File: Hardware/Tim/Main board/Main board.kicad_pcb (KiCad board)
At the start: 4 copper layers, 120.9 x 66.6 mm, 184 parts, among them J1 SOICbite, J10 Conn_01x03_Socket, J11 Conn_01x02_Pin, J12 USB_C_Receptacle_USB2.0, J13 Conn_01x02_Socket, J14 Conn_01x02_Pin, J15 Conn_01x04_Socket, J16 Conn_01x02_Pin, J17 Conn_01x04_Pin, J18 Conn_01x03_Socket, J2 USB_C_Receptacle_USB2.0, J3 Conn_01x04_Socket, J4 Conn_01x04_Socket, J5 Conn_01x04_Socket, J6 Conn_01x02_Socket, J7 Conn_01x02_Socket, J8 U.FL, J9 SOICbite, Q1 IRLML0060TRPBF, Q2 IRLML0060TRPBF, U1 RP2040, U10 MAX-M10S, U11 ADP7105ACPZ-5.0-R7, U12 ADP7105ACPZ-3.3-R7, U13 ADP7105ACPZ-5.0-R7, U14 TPS2121RUXR, U15 TPS2121RUXR, U2 W25Q64JVZP, U3 MS5607-02BA, U4 BMI270, U5 ADP7105ACPZ-3.3-R7, U6 DRF1262TL, U7 RP2040, U8 W25Q64JVZP, Y1 12MHz, Y2 12MHz

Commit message: Double checking everything is pushed
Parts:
- added J19: Micro_SD_Card, BPPlib:JAE_ST1W008S4ER1500, F.Cu at (99.0, 108.8)
- added J20: Micro_SD_Card, BPPlib:JAE_ST1W008S4ER1500, F.Cu at (154.6, 102.0)
- added REF**: MountingHole_3.2mm_M3, MountingHole:MountingHole_3.2mm_M3, F.Cu at (174.0, 83.0)
- moved AE1 38.2 mm to (59.2, 114.5), turned to -90 degrees
- moved J15 34.3 mm to (96.4, 114.8), turned to 0 degrees
- moved JP3 29.5 mm to (98.2, 110.2)
- moved J18 29.1 mm to (84.2, 114.5), turned to 0 degrees
- moved JP4 26.5 mm to (94.3, 110.2), turned to 180 degrees
- moved REF** 26.4 mm to (131.0, 105.0)
- moved U10 25.3 mm to (73.2, 113.8), turned to 180 degrees
- moved J7 24.3 mm to (61.8, 102.2), turned to -90 degrees
- moved J6 24.0 mm to (61.8, 93.5), turned to -90 degrees
- moved C57 20.0 mm to (70.8, 107.4), turned to 180 degrees
- moved R63 19.3 mm to (65.6, 92.8), turned to -90 degrees
- moved R44 18.6 mm to (65.7, 101.4), turned to -90 degrees
- moved BT1 15.2 mm to (72.1, 103.5), turned to -90 degrees
- moved C59 14.2 mm to (82.0, 101.0), turned to 180 degrees
- moved R12 13.8 mm to (76.8, 106.5), turned to 180 degrees
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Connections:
- U1 pad 32: /TXEN -> /SPI0_CS_SD
- U1 pad 38: /EXTINT -> /TXEN
- U7 pad 15: unconnected-(U7-GPIO12-Pad15) -> /SPI0_POCI_R
- U7 pad 16: unconnected-(U7-GPIO13-Pad16) -> /SPI0_CS_SD_R
- U7 pad 17: unconnected-(U7-GPIO14-Pad17) -> /SPI0_SCK_R
- U7 pad 18: unconnected-(U7-GPIO15-Pad18) -> /SPI0_PICO_R
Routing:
- net /DIR: track 110.2 -> 59.2 mm, vias 6 -> 3
- net /STEP: track 107.7 -> 58.7 mm, vias 6 -> 3
- net GND: track 335.8 -> 384.0 mm, vias 41 -> 46
- net /SPI0_POCI_R: track 0.00 -> 42.9 mm
- net /EXTINT: track 42.0 -> 0.00 mm, vias 2 -> 0
- net /SPI0_CS_SD_R: track 0.00 -> 40.7 mm, vias 0 -> 2
- net /SPI0_CS_SD: track 0.00 -> 39.9 mm, vias 0 -> 2
- net /SPI0_SCK_R: track 0.00 -> 39.5 mm
- net /SPI0_PICO_R: track 0.00 -> 36.0 mm
- net /SPI0_PICO: track 39.1 -> 71.4 mm, vias 2 -> 3
- net /SPI0_SCK: track 41.8 -> 72.6 mm, vias 2 -> 4
- net /TIMEPULSE: track 42.9 -> 71.6 mm
- net +5V: track 81.5 -> 108.5 mm, vias 0 -> 4
- net /SPI0_POCI: track 35.5 -> 62.0 mm, vias 2 -> 3
- net Net-(J13-Pin_2): track 29.9 -> 55.3 mm, vias 2 -> 0
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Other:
- board size 120.9 x 66.6 mm -> 121 x 66.5 mm
- board text added: "WayWayWay"

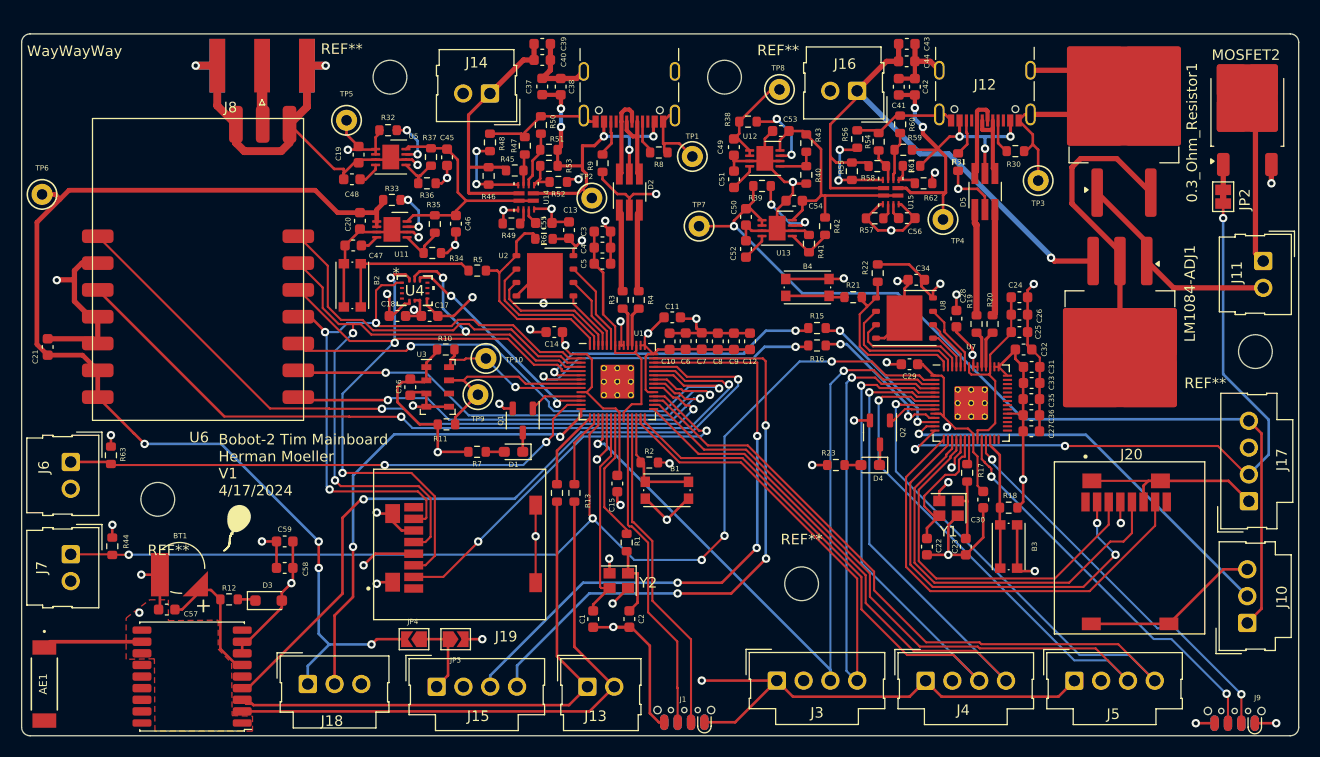
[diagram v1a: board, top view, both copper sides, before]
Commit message: Pressure temp done if so inclined add 2nd order compensation
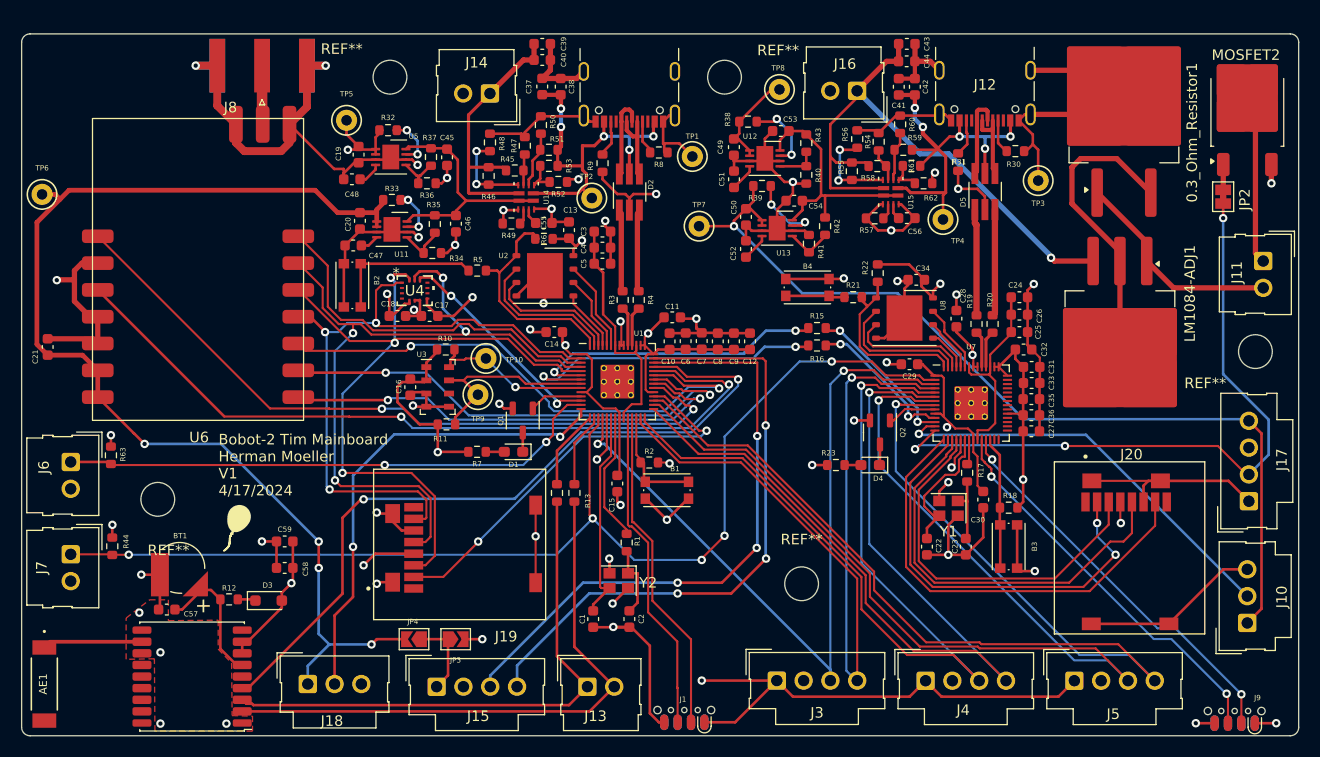
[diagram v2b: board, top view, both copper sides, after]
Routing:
- net GND: vias 46 -> 49
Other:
- board text removed: "WayWayWay"
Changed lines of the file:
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@@
 			(outputformat 1)
 			(mirror no)
-			(drillshape 1)
+			(drillshape 0)
 			(scaleselection 1)
-			(outputdirectory "")
+			(outputdirectory "./")
 		)
 	)
@@
 			(size 1.084435 1.084435)
 			(layers "F.Paste")
-			(roundrect_rratio 0.230535)
+			(roundrect_rratio 0.2305347946)
 		)
 		(pad "" smd roundrect
@@
 			(size 1.084435 1.084435)
 			(layers "F.Paste")
-			(roundrect_rratio 0.230535)
+			(roundrect_rratio 0.2305347946)
 		)
 		(pad "" smd roundrect
@@
 			(size 1.084435 1.084435)
 			(layers "F.Paste")
-			(roundrect_rratio 0.230535)
+			(roundrect_rratio 0.2305347946)
 		)
 		(pad "" smd roundrect
@@
 			(size 1.084435 1.084435)
 			(layers "F.Paste")
-			(roundrect_rratio 0.230535)
+			(roundrect_rratio 0.2305347946)
 		)
 		(pad "1" smd roundrect
@@
 			(layers "*.Cu" "*.Mask")
 			(remove_unused_layers no)
-			(roundrect_rratio 0.143678)
+			(roundrect_rratio 0.1436781609)
 			(net 9 "+5V")
 			(pinfunction "Pin_1")
@@
 			(layers "*.Cu" "*.Mask")
 			(remove_unused_layers no)
-			(roundrect_rratio 0.143678)
+			(roundrect_rratio 0.1436781609)
 			(net 16 "+BATT")
 			(pinfunction "Pin_1")
@@
 			(layers "*.Cu" "*.Mask")
 			(remove_unused_layers no)
-			(roundrect_rratio 0.143678)
+			(roundrect_rratio 0.1436781609)
 			(net 6 "+3V3")
 			(pinfunction "Pin_1")
@@
 			(size 1.084435 1.084435)
 			(layers "F.Paste")
-			(roundrect_rratio 0.230535)
+			(roundrect_rratio 0.2305347946)
 		)
 		(pad "" smd roundrect
@@
 			(size 1.084435 1.084435)
 			(layers "F.Paste")
-			(roundrect_rratio 0.230535)
+			(roundrect_rratio 0.2305347946)
 		)
 		(pad "" smd roundrect
@@
 			(size 1.084435 1.084435)
 			(layers "F.Paste")
-			(roundrect_rratio 0.230535)
+			(roundrect_rratio 0.2305347946)
 		)
 		(pad "" smd roundrect
@@
 			(size 1.084435 1.084435)
 			(layers "F.Paste")
-			(roundrect_rratio 0.230535)
+			(roundrect_rratio 0.2305347946)
 		)
 		(pad "1" smd roundrect
@@
 			(size 4.6 1.1)
 			(layers "F.Cu" "F.Paste" "F.Mask")
-			(roundrect_rratio 0.227273)
+			(roundrect_rratio 0.2272727273)
 			(net 170 "Net-(J11-Pin_2)")
 			(pinfunction "ADJ")
@@
 			(size 4.6 1.1)
 			(layers "F.Cu" "F.Paste" "F.Mask")
-			(roundrect_rratio 0.227273)
+			(roundrect_rratio 0.2272727273)
 			(net 169 "Net-(LM1084-ADJ1-VO)")
 			(pinfunction "VO")
@@
 			(size 4.55 5.25)
 			(layers "F.Cu" "F.Paste")
-			(roundrect_rratio 0.054945)
+			(roundrect_rratio 0.05494505495)
 			(net 169 "Net-(LM1084-ADJ1-VO)")
 			(pinfunction "VO")
@@
 			(size 4.55 5.25)
 			(layers "F.Cu" "F.Paste")
-			(roundrect_rratio 0.054945)
+			(roundrect_rratio 0.05494505495)
 			(net 169 "Net-(LM1084-ADJ1-VO)")
 			(pinfunction "VO")
@@
 			(size 9.4 10.8)
 			(layers "F.Cu" "F.Mask")
-			(roundrect_rratio 0.026596)
+			(roundrect_rratio 0.02659595745)
 			(net 169 "Net-(LM1084-ADJ1-VO)")
 			(pinfunction "VO")
@@
 			(size 4.55 5.25)
 			(layers "F.Cu" "F.Paste")
-			(roundrect_rratio 0.054945)
+			(roundrect_rratio 0.05494505495)
 			(net 169 "Net-(LM1084-ADJ1-VO)")
 			(pinfunction "VO")
@@
 			(size 4.55 5.25)
 			(layers "F.Cu" "F.Paste")
-			(roundrect_rratio 0.054945)
+			(roundrect_rratio 0.05494505495)
 			(net 169 "Net-(LM1084-ADJ1-VO)")
 			(pinfunction "VO")
@@
 			(size 4.6 1.1)
 			(layers "F.Cu" "F.Paste" "F.Mask")
-			(roundrect_rratio 0.227273)
+			(roundrect_rratio 0.2272727273)
 			(net 16 "+BATT")
 			(pinfunction "VI")
@@
 			(layers "*.Cu" "*.Mask")
 			(remove_unused_layers no)
-			(roundrect_rratio 0.143678)
+			(roundrect_rratio 0.1436781609)
 			(net 92 "/LS2")
 			(pinfunction "Pin_1")
@@
 			(size 2.2 1.2)
 			(layers "F.Cu" "F.Paste" "F.Mask")
-			(roundrect_rratio 0.208333)
+			(roundrect_rratio 0.2083333333)
 			(net 172 "Net-(JP2-B)")
 			(pinfunction "G")
@@
 			(size 3.05 2.75)
 			(layers "F.Cu" "F.Paste")
-			(roundrect_rratio 0.090909)
+			(roundrect_rratio 0.09090909091)
 			(net 171 "Net-(J11-Pin_1)")
 			(pinfunction "D")
@@
 			(size 3.05 2.75)
 			(layers "F.Cu" "F.Paste")
-			(roundrect_rratio 0.090909)
+			(roundrect_rratio 0.09090909091)
 			(net 171 "Net-(J11-Pin_1)")
 			(pinfunction "D")
@@
 			(size 6.4 5.8)
 			(layers "F.Cu" "F.Mask")
-			(roundrect_rratio 0.043103)
+			(roundrect_rratio 0.04310293103)
 			(net 171 "Net-(J11-Pin_1)")
 			(pinfunction "D")
@@
 			(size 3.05 2.75)
 			(layers "F.Cu" "F.Paste")
-			(roundrect_rratio 0.090909)
+			(roundrect_rratio 0.09090909091)
 			(net 171 "Net-(J11-Pin_1)")
 			(pinfunction "D")
@@
 			(size 3.05 2.75)
 			(layers "F.Cu" "F.Paste")
-			(roundrect_rratio 0.090909)
+			(roundrect_rratio 0.09090909091)
 			(net 171 "Net-(J11-Pin_1)")
 			(pinfunction "D")
@@
 			(size 2.2 1.2)
 			(layers "F.Cu" "F.Paste" "F.Mask")
-			(roundrect_rratio 0.208333)
+			(roundrect_rratio 0.2083333333)
 			(net 1 "GND")
 			(pinfunction "S")
@@
 			(layers "*.Cu" "*.Mask")
 			(remove_unused_layers no)
-			(roundrect_rratio 0.143678)
+			(roundrect_rratio 0.1436781609)
 			(net 148 "Net-(J14-Pin_1)")
 			(pinfunction "Pin_1")
@@
 			(size 1.37 1.73)
 			(layers "F.Paste")
-			(roundrect_rratio 0.182482)
+			(roundrect_rratio 0.1824817518)
 		)
 		(pad "" smd roundrect
@@
 			(size 1.37 1.73)
 			(layers "F.Paste")
-			(roundrect_rratio 0.182482)
+			(roundrect_rratio 0.1824817518)
 		)
 		(pad "" smd roundrect
@@
 			(size 1.37 1.73)
 			(layers "F.Paste")
-			(roundrect_rratio 0.182482)
+			(roundrect_rratio 0.1824817518)
 		)
 		(pad "" smd roundrect
@@
 			(size 1.37 1.73)
 			(layers "F.Paste")
-			(roundrect_rratio 0.182482)
+			(roundrect_rratio 0.1824817518)
 		)
 		(pad "1" smd roundrect
@@
 			(layers "*.Cu" "*.Mask")
 			(remove_unused_layers no)
-			(roundrect_rratio 0.143678)
+			(roundrect_rratio 0.1436781609)
 			(net 168 "+5V_R")
 			(pinfunction "Pin_1")
@@
 			(layers "*.Cu" "*.Mask")
 			(remove_unused_layers no)
-			(roundrect_rratio 0.143678)
+			(roundrect_rratio 0.1436781609)
 			(net 171 "Net-(J11-Pin_1)")
 			(pinfunction "Pin_1")
@@
 			(size 4.6 1.1)
 			(layers "F.Cu" "F.Paste" "F.Mask")
-			(roundrect_rratio 0.227273)
+			(roundrect_rratio 0.2272727273)
 			(net 170 "Net-(J11-Pin_2)")
 			(pintype "passive")
@@
 			(size 4.6 1.1)
 			(layers "F.Cu" "F.Paste" "F.Mask")
-			(roundrect_rratio 0.227273)
+			(roundrect_rratio 0.2272727273)
 			(net 169 "Net-(LM1084-ADJ1-VO)")
 			(pintype "passive")
@@
 			(size 4.55 5.25)
 			(layers "F.Cu" "F.Paste")
-			(roundrect_rratio 0.054945)
+			(roundrect_rratio 0.05494505495)
 			(net 1 "GND")
 			(pinfunction "Gnd")
@@
 			(size 4.55 5.25)
 			(layers "F.Cu" "F.Paste")
-			(roundrect_rratio 0.054945)
+			(roundrect_rratio 0.05494505495)
 			(net 1 "GND")
 			(pinfunction "Gnd")
@@
 			(size 9.4 10.8)
 			(layers "F.Cu" "F.Mask")
-			(roundrect_rratio 0.026596)
+			(roundrect_rratio 0.02659595745)
 			(net 1 "GND")
 			(pinfunction "Gnd")
@@
 			(size 4.55 5.25)
 			(layers "F.Cu" "F.Paste")
-			(roundrect_rratio 0.054945)
+			(roundrect_rratio 0.05494505495)
 			(net 1 "GND")
 			(pinfunction "Gnd")
@@
 			(size 4.55 5.25)
 			(layers "F.Cu" "F.Paste")
-			(roundrect_rratio 0.054945)
+			(roundrect_rratio 0.05494505495)
 			(net 1 "GND")
 			(pinfunction "Gnd")
@@
 			(layers "*.Cu" "*.Mask")
 			(remove_unused_layers no)
-			(roundrect_rratio 0.143678)
+			(roundrect_rratio 0.1436781609)
 			(net 101 "Net-(J15-Pin_1)")
 			(pinfunction "Pin_1")
@@
 			(layers "*.Cu" "*.Mask")
 			(remove_unused_layers no)
-			(roundrect_rratio 0.143678)
+			(roundrect_rratio 0.1436781609)
 			(net 50 "/LS1")
 			(pinfunction "Pin_1")
@@
 			(size 1.37 1.73)
 			(layers "F.Paste")
-			(roundrect_rratio 0.182482)
+			(roundrect_rratio 0.1824817518)
 		)
 		(pad "" smd roundrect
@@
 			(size 1.37 1.73)
 			(layers "F.Paste")
-			(roundrect_rratio 0.182482)
+			(roundrect_rratio 0.1824817518)
 		)
 		(pad "" smd roundrect
@@
 			(size 1.37 1.73)
 			(layers "F.Paste")
-			(roundrect_rratio 0.182482)
+			(roundrect_rratio 0.1824817518)
 		)
 		(pad "" smd roundrect
@@
 			(size 1.37 1.73)
 			(layers "F.Paste")
-			(roundrect_rratio 0.182482)
+			(roundrect_rratio 0.1824817518)
 		)
 		(pad "1" smd roundrect
@@
 			(layers "*.Cu" "*.Mask")
 			(remove_unused_layers no)
-			(roundrect_rratio 0.143678)
+			(roundrect_rratio 0.1436781609)
 			(net 61 "Net-(J13-Pin_1)")
 			(pinfunction "Pin_1")
@@
 			(layers "*.Cu" "*.Mask")
 			(remove_unused_layers no)
-			(roundrect_rratio 0.143678)
+			(roundrect_rratio 0.1436781609)
 			(net 6 "+3V3")
 			(pinfunction "Pin_1")
@@
 			(layers "*.Cu" "*.Mask")
 			(remove_unused_layers no)
-			(roundrect_rratio 0.143678)
+			(roundrect_rratio 0.1436781609)
 			(net 1 "GND")
 			(pinfunction "Pin_1")
@@
 			(layers "*.Cu" "*.Mask")
 			(remove_unused_layers no)
-			(roundrect_rratio 0.143678)
+			(roundrect_rratio 0.1436781609)
 			(net 6 "+3V3")
 			(pinfunction "Pin_1")
@@
 		(layer "Edge.Cuts")
 	)
-	(gr_text "WayWayWay"
-		(at 57.6072 55.118 0)
-		(layer "F.SilkS")
-		(effects
-			(font
-				(size 1 1)
-				(thickness 0.15)
-			)
-			(justify left bottom)
-		)
-	)
 	(gr_text "Bobot-2 Tim Mainboard\nHerman Moeller\nV1\n4/17/2024"
 		(at 75.75 96.75 0)
@@
 	)
 	(via
+		(at 70.25 111.5)
+		(size 0.8)
+		(drill 0.4)
+		(layers "F.Cu" "B.Cu")
+		(free yes)
+		(net 1)
+	)
+	(via
 		(at 113.0935 106.8705)
 		(size 0.8)
@@
 	)
 	(via
+		(at 70.25 118.25)
+		(size 0.8)
+		(drill 0.4)
+		(layers "F.Cu" "B.Cu")
+		(free yes)
+		(net 1)
+	)
+	(via
 		(at 68.25 107.735462)
 		(size 0.8)
@@
 		(net 1)
 	)
+	(via
+		(at 76.5 118.25)
+		(size 0.8)
+		(drill 0.4)
+		(layers "F.Cu" "B.Cu")
+		(free yes)
+		(net 1)
+	)
